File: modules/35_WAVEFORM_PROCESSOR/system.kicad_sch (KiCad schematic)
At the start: 8 parts, among them J1 Card_Connector, J2 ES1, J3 ES2, J4 CM, J5 OUT

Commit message: waveform processor updates
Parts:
- J2: value ES1 -> Mono_Jack; Legend (none) -> ES1
- J3: value ES2 -> Mono_Jack; Legend (none) -> ES2
- J4: value CM -> Mono_Jack; Legend (none) -> CM
- J5: value OUT -> Mono_Jack; Legend (none) -> OUT
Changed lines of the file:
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@@
 			)
 		)
-		(property "Value" "ES1"
-			(at 162.56 116.2049 0)
-			(show_name no)
-			(do_not_autoplace no)
-			(effects
-				(font
-					(size 1.27 1.27)
-				)
-				(justify left)
+		(property "Value" "Mono_Jack"
+			(at 157.48 119.126 0)
+			(hide yes)
+			(show_name no)
+			(do_not_autoplace no)
+			(effects
+				(font
+					(size 1.27 1.27)
+				)
 			)
 		)
@@
 					(size 1.27 1.27)
 				)
+			)
+		)
+		(property "Legend" "ES1"
+			(at 162.56 116.2049 0)
+			(show_name no)
+			(do_not_autoplace no)
+			(effects
+				(font
+					(size 1.27 1.27)
+				)
+				(justify left)
 			)
 		)
@@
 			)
 		)
-		(property "Value" "OUT"
-			(at 162.56 154.3049 0)
-			(show_name no)
-			(do_not_autoplace no)
-			(effects
-				(font
-					(size 1.27 1.27)
-				)
-				(justify left)
+		(property "Value" "Mono_Jack"
+			(at 157.48 157.226 0)
+			(hide yes)
+			(show_name no)
+			(do_not_autoplace no)
+			(effects
+				(font
+					(size 1.27 1.27)
+				)
 			)
 		)
@@
 					(size 1.27 1.27)
 				)
+			)
+		)
+		(property "Legend" "OUT"
+			(at 162.56 154.3049 0)
+			(show_name no)
+			(do_not_autoplace no)
+			(effects
+				(font
+					(size 1.27 1.27)
+				)
+				(justify left)
 			)
 		)
@@
 			)
 		)
-		(property "Value" "CM"
-			(at 162.56 141.6049 0)
-			(show_name no)
-			(do_not_autoplace no)
-			(effects
-				(font
-					(size 1.27 1.27)
-				)
-				(justify left)
+		(property "Value" "Mono_Jack"
+			(at 157.48 144.526 0)
+			(hide yes)
+			(show_name no)
+			(do_not_autoplace no)
+			(effects
+				(font
+					(size 1.27 1.27)
+				)
 			)
 		)
@@
 					(size 1.27 1.27)
 				)
+			)
+		)
+		(property "Legend" "CM"
+			(at 162.56 141.6049 0)
+			(show_name no)
+			(do_not_autoplace no)
+			(effects
+				(font
+					(size 1.27 1.27)
+				)
+				(justify left)
 			)
 		)
@@
 			)
 		)
-		(property "Value" "ES2"
-			(at 162.56 128.9049 0)
-			(show_name no)
-			(do_not_autoplace no)
-			(effects
-				(font
-					(size 1.27 1.27)
-				)
-				(justify left)
+		(property "Value" "Mono_Jack"
+			(at 157.48 131.826 0)
+			(hide yes)
+			(show_name no)
+			(do_not_autoplace no)
+			(effects
+				(font
+					(size 1.27 1.27)
+				)
 			)
 		)
@@
 			)
 		)
+		(property "Legend" "ES2"
+			(at 162.56 128.9049 0)
+			(show_name no)
+			(do_not_autoplace no)
+			(effects
+				(font
+					(size 1.27 1.27)
+				)
+				(justify left)
+			)
+		)

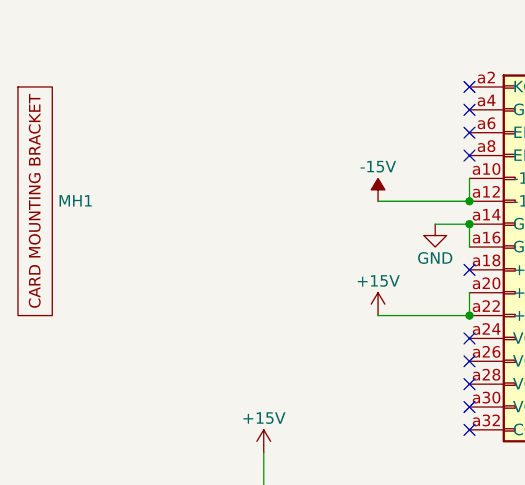
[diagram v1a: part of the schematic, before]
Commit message: fixed card bracket footprint
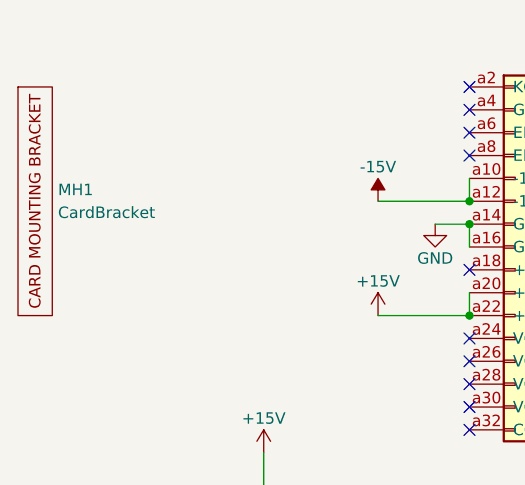
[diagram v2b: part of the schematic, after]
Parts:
- MH1: value (none) -> CardBracket; footprint FormantKO:Schroff_60807-011_3U_Pair -> FormantKO:Card_Bracket
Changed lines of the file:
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@@
 		(fields_autoplaced yes)
 		(property "Reference" "MH1"
-			(at 78.74 63.4999 0)
+			(at 78.74 62.2299 0)
 			(show_name no)
 			(do_not_autoplace no)
@@
 			)
 		)
-		(property "Value" ""
-			(at 76.2 63.5 0)
+		(property "Value" "CardBracket"
+			(at 78.74 64.7699 0)
 			(show_name no)
 			(do_not_autoplace no)
@@
 					(size 1.27 1.27)
 				)
+				(justify left)
 			)
 		)
-		(property "Footprint" "FormantKO:Schroff_60807-011_3U_Pair"
+		(property "Footprint" "FormantKO:Card_Bracket"
 			(at 76.2 63.5 0)
 			(hide yes)
